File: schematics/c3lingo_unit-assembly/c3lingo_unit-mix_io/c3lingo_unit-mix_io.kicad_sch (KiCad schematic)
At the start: 40 parts, among them J201 Stage Line-In, J202 Mix Line-Out, J203 PowerSupply, J204 Inputs, J205 Output, U201 LM833N, U202 DRV134PA, U203 LM833N

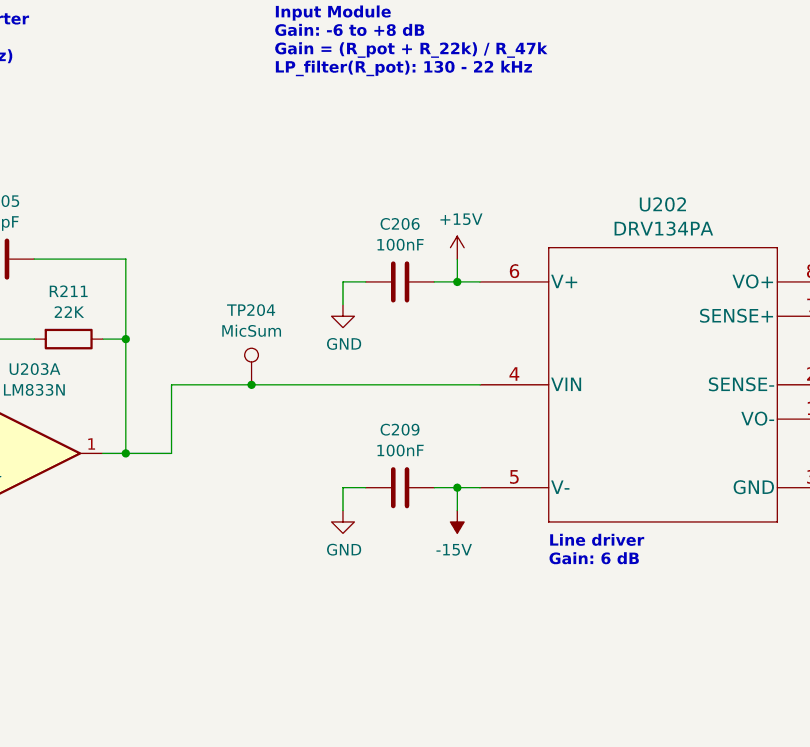
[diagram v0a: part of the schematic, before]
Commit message: Schematics: Fix multiple issues with initial prototype
- Removed high-pass filter between microphone pre-amp and gain as it made things sound worse
- Removed low-pass filter before VU meter as it looked fine without
- Connect VU meter to +15 V directly as 5 V didn't work
- Footprint of the gain potentiometer (Alps RK09) seems to be fixed with the KiCad 6 library
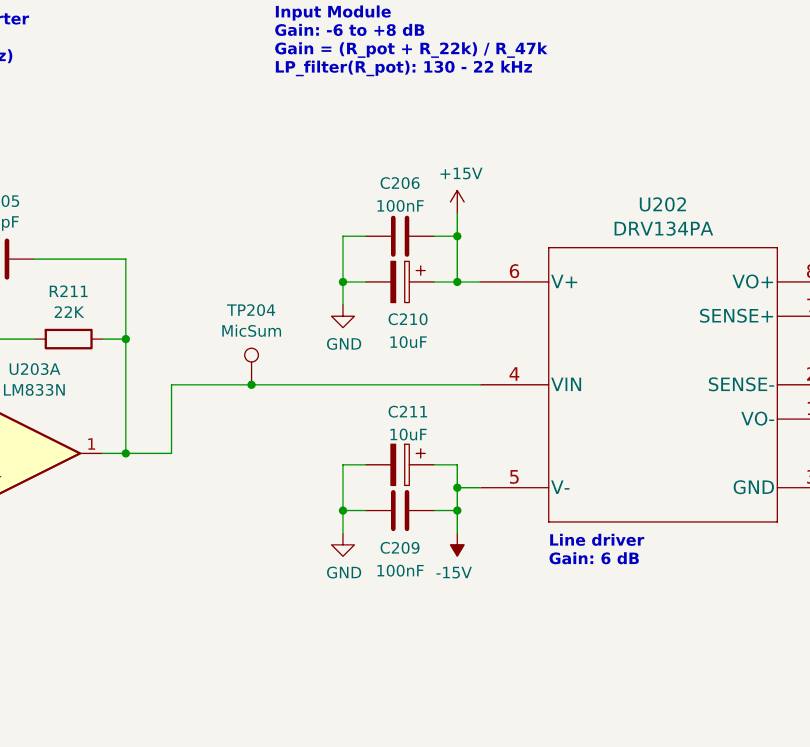
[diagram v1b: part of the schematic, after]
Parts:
- added C210, C211: 10uF, Capacitor_THT:CP_Radial_D5.0mm_P2.00mm, symbol Device:C_Polarized
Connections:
- net +15V: now also C210.1
- net -15V: now also C211.1
- net GND: now also C210.2, C211.2
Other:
- moved on the sheet: C206, C209

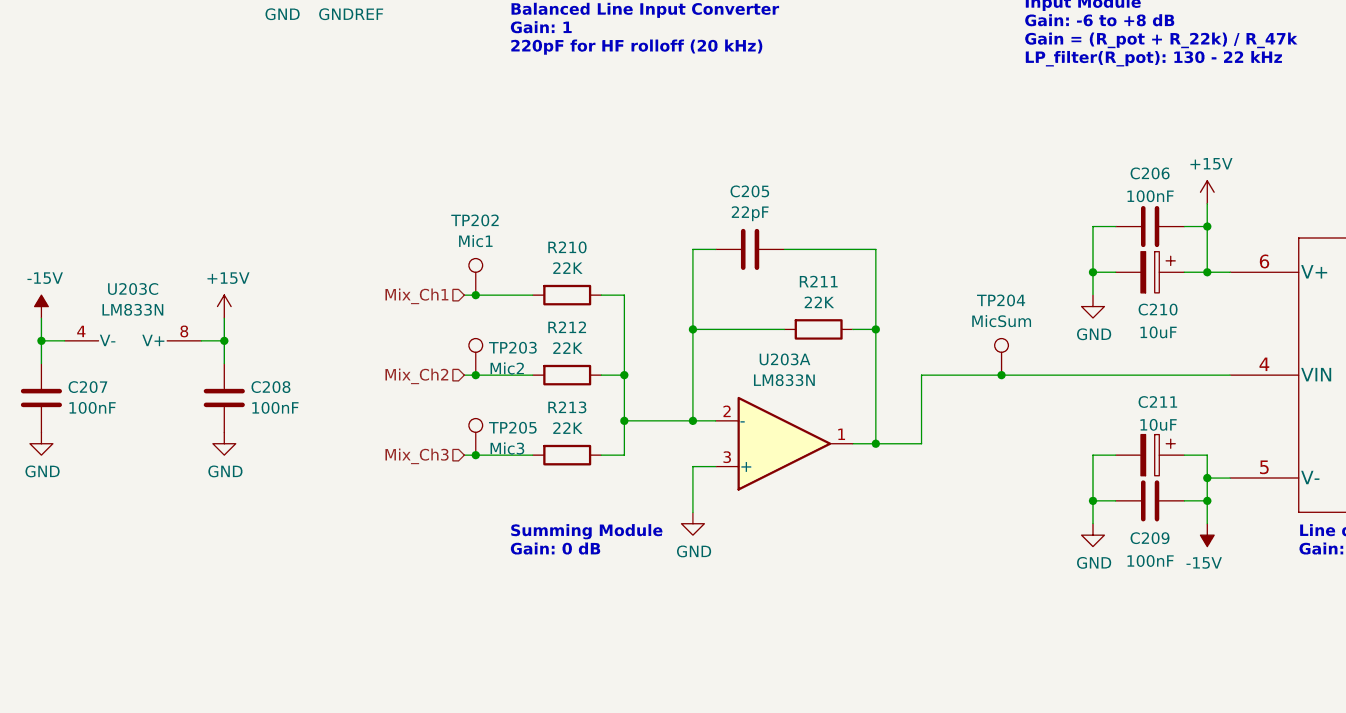
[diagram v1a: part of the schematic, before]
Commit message: [TIDY] Split channel into two schematics
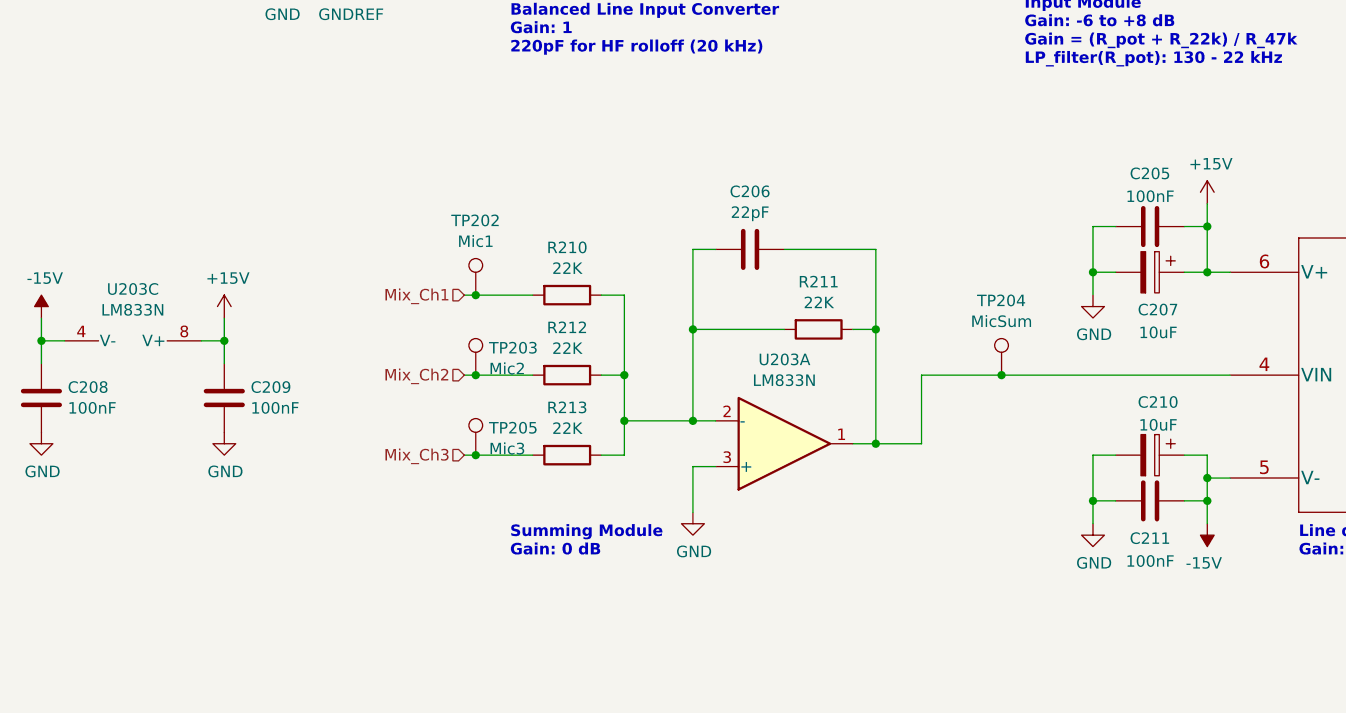
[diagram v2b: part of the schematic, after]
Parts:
- U202: footprint Package_DIP:DIP-8_W7.62mm_Socket_LongPads -> Package_DIP:DIP-8_W7.62mm
- renumbered C206 to C205, C205 to C206, C210 to C207, C207 to C208, C208 to C209, C211 to C210, C209 to C211
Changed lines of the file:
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@@
   (symbol (lib_id "Device:C") (at 27.94 116.84 180) (unit 1)
     (in_bom yes) (on_board yes)
-    (property "Reference" "C207" (id 0) (at 30.861 115.6716 0)
+    (property "Reference" "C208" (id 0) (at 30.861 115.6716 0)
       (effects (font (size 1.27 1.27)) (justify right))
     )
@@
   (symbol (lib_id "Device:C") (at 48.26 116.84 180) (unit 1)
     (in_bom yes) (on_board yes)
-    (property "Reference" "C208" (id 0) (at 51.181 115.6716 0)
+    (property "Reference" "C209" (id 0) (at 51.181 115.6716 0)
       (effects (font (size 1.27 1.27)) (justify right))
     )
@@
   (symbol (lib_id "Device:C") (at 106.68 100.33 270) (unit 1)
     (in_bom yes) (on_board yes)
-    (property "Reference" "C205" (id 0) (at 106.68 93.9292 90))
+    (property "Reference" "C206" (id 0) (at 106.68 93.9292 90))
     (property "Value" "22pF" (id 1) (at 106.68 96.2406 90))
     (property "Footprint" "Capacitor_THT:C_Disc_D5.0mm_W2.5mm_P5.00mm" (id 2) (at 102.87 101.2952 0)
@@
   (symbol (lib_id "power:GND") (at 100.33 129.54 0) (unit 1)
     (in_bom yes) (on_board yes)
-    (property "Reference" "#PWR0220" (id 0) (at 100.33 135.89 0)
+    (property "Reference" "#PWR0218" (id 0) (at 100.33 135.89 0)
       (effects (font (size 1.27 1.27)) hide)
     )
@@
       (effects (font (size 1.524 1.524)))
     )
-    (property "Footprint" "Package_DIP:DIP-8_W7.62mm_Socket_LongPads" (id 2) (at 180.34 98.044 0)
+    (property "Footprint" "Package_DIP:DIP-8_W7.62mm" (id 2) (at 180.34 98.044 0)
       (effects (font (size 1.524 1.524)) hide)
     )
@@
   (symbol (lib_id "power:-15V") (at 157.48 130.81 180) (unit 1)
     (in_bom yes) (on_board yes)
-    (property "Reference" "#PWR0218" (id 0) (at 157.48 133.35 0)
+    (property "Reference" "#PWR0220" (id 0) (at 157.48 133.35 0)
       (effects (font (size 1.27 1.27)) hide)
     )
@@
   (symbol (lib_id "power:GND") (at 144.78 130.81 0) (unit 1)
     (in_bom yes) (on_board yes)
-    (property "Reference" "#PWR0217" (id 0) (at 144.78 137.16 0)
+    (property "Reference" "#PWR0219" (id 0) (at 144.78 137.16 0)
       (effects (font (size 1.27 1.27)) hide)
     )
@@
   (symbol (lib_id "Device:C") (at 151.13 128.27 270) (unit 1)
     (in_bom yes) (on_board yes) (fields_autoplaced)
-    (property "Reference" "C209" (id 0) (at 151.13 132.4594 90))
+    (property "Reference" "C211" (id 0) (at 151.13 132.4594 90))
     (property "Value" "100nF" (id 1) (at 151.13 134.9963 90))
     (property "Footprint" "Capacitor_THT:C_Disc_D5.0mm_W2.5mm_P5.00mm" (id 2) (at 147.32 129.2352 0)
@@
   (symbol (lib_id "Device:C") (at 151.13 97.79 270) (unit 1)
     (in_bom yes) (on_board yes) (fields_autoplaced)
-    (property "Reference" "C206" (id 0) (at 151.13 91.9312 90))
+    (property "Reference" "C205" (id 0) (at 151.13 91.9312 90))
     (property "Value" "100nF" (id 1) (at 151.13 94.4681 90))
     (property "Footprint" "Capacitor_THT:C_Disc_D5.0mm_W2.5mm_P5.00mm" (id 2) (at 147.32 98.7552 0)
@@
   (symbol (lib_id "power:GND") (at 203.2 128.27 0) (unit 1)
     (in_bom yes) (on_board yes)
-    (property "Reference" "#PWR0219" (id 0) (at 203.2 134.62 0)
+    (property "Reference" "#PWR0217" (id 0) (at 203.2 134.62 0)
       (effects (font (size 1.27 1.27)) hide)
     )
@@
   (symbol (lib_id "Device:C_Polarized") (at 151.13 123.19 270) (unit 1)
     (in_bom yes) (on_board yes) (fields_autoplaced)
-    (property "Reference" "C211" (id 0) (at 152.019 117.3312 90))
+    (property "Reference" "C210" (id 0) (at 152.019 117.3312 90))
     (property "Value" "10uF" (id 1) (at 152.019 119.8681 90))
     (property "Footprint" "Capacitor_THT:CP_Radial_D5.0mm_P2.00mm" (id 2) (at 147.32 124.1552 0)
@@
   (symbol (lib_id "Device:C_Polarized") (at 151.13 102.87 270) (unit 1)
     (in_bom yes) (on_board yes) (fields_autoplaced)
-    (property "Reference" "C210" (id 0) (at 152.019 107.0594 90))
+    (property "Reference" "C207" (id 0) (at 152.019 107.0594 90))
     (property "Value" "10uF" (id 1) (at 152.019 109.5963 90))
     (property "Footprint" "Capacitor_THT:CP_Radial_D5.0mm_P2.00mm" (id 2) (at 147.32 103.8352 0)
@@
       (reference "C204") (unit 1) (value "100nF") (footprint "Capacitor_THT:C_Disc_D5.0mm_W2.5mm_P5.00mm")
     )
+    (path "/00000000-0000-0000-0000-0000604659b0"
+      (reference "C205") (unit 1) (value "100nF") (footprint "Capacitor_THT:C_Disc_D5.0mm_W2.5mm_P5.00mm")
+    )
     (path "/00000000-0000-0000-0000-00005fd269db"
-      (reference "C205") (unit 1) (value "22pF") (footprint "Capacitor_THT:C_Disc_D5.0mm_W2.5mm_P5.00mm")
-    )
-    (path "/00000000-0000-0000-0000-0000604659b0"
-      (reference "C206") (unit 1) (value "100nF") (footprint "Capacitor_THT:C_Disc_D5.0mm_W2.5mm_P5.00mm")
+      (reference "C206") (unit 1) (value "22pF") (footprint "Capacitor_THT:C_Disc_D5.0mm_W2.5mm_P5.00mm")
+    )
+    (path "/9feded9d-6d07-46f0-97ed-4e08902d2588"
+      (reference "C207") (unit 1) (value "10uF") (footprint "Capacitor_THT:CP_Radial_D5.0mm_P2.00mm")
     )
     (path "/00000000-0000-0000-0000-00005fcf1264"
-      (reference "C207") (unit 1) (value "100nF") (footprint "Capacitor_THT:C_Disc_D5.0mm_W2.5mm_P5.00mm")
+      (reference "C208") (unit 1) (value "100nF") (footprint "Capacitor_THT:C_Disc_D5.0mm_W2.5mm_P5.00mm")
     )
     (path "/00000000-0000-0000-0000-00005fcf126a"
-      (reference "C208") (unit 1) (value "100nF") (footprint "Capacitor_THT:C_Disc_D5.0mm_W2.5mm_P5.00mm")
+      (reference "C209") (unit 1) (value "100nF") (footprint "Capacitor_THT:C_Disc_D5.0mm_W2.5mm_P5.00mm")
+    )
+    (path "/36f80211-7578-4f7e-b084-5c1e7cfd5788"
+      (reference "C210") (unit 1) (value "10uF") (footprint "Capacitor_THT:CP_Radial_D5.0mm_P2.00mm")
     )
     (path "/00000000-0000-0000-0000-000060444365"
-      (reference "C209") (unit 1) (value "100nF") (footprint "Capacitor_THT:C_Disc_D5.0mm_W2.5mm_P5.00mm")
+      (reference "C211") (unit 1) (value "100nF") (footprint "Capacitor_THT:C_Disc_D5.0mm_W2.5mm_P5.00mm")
     )
     (path "/00000000-0000-0000-0000-00006148253b"

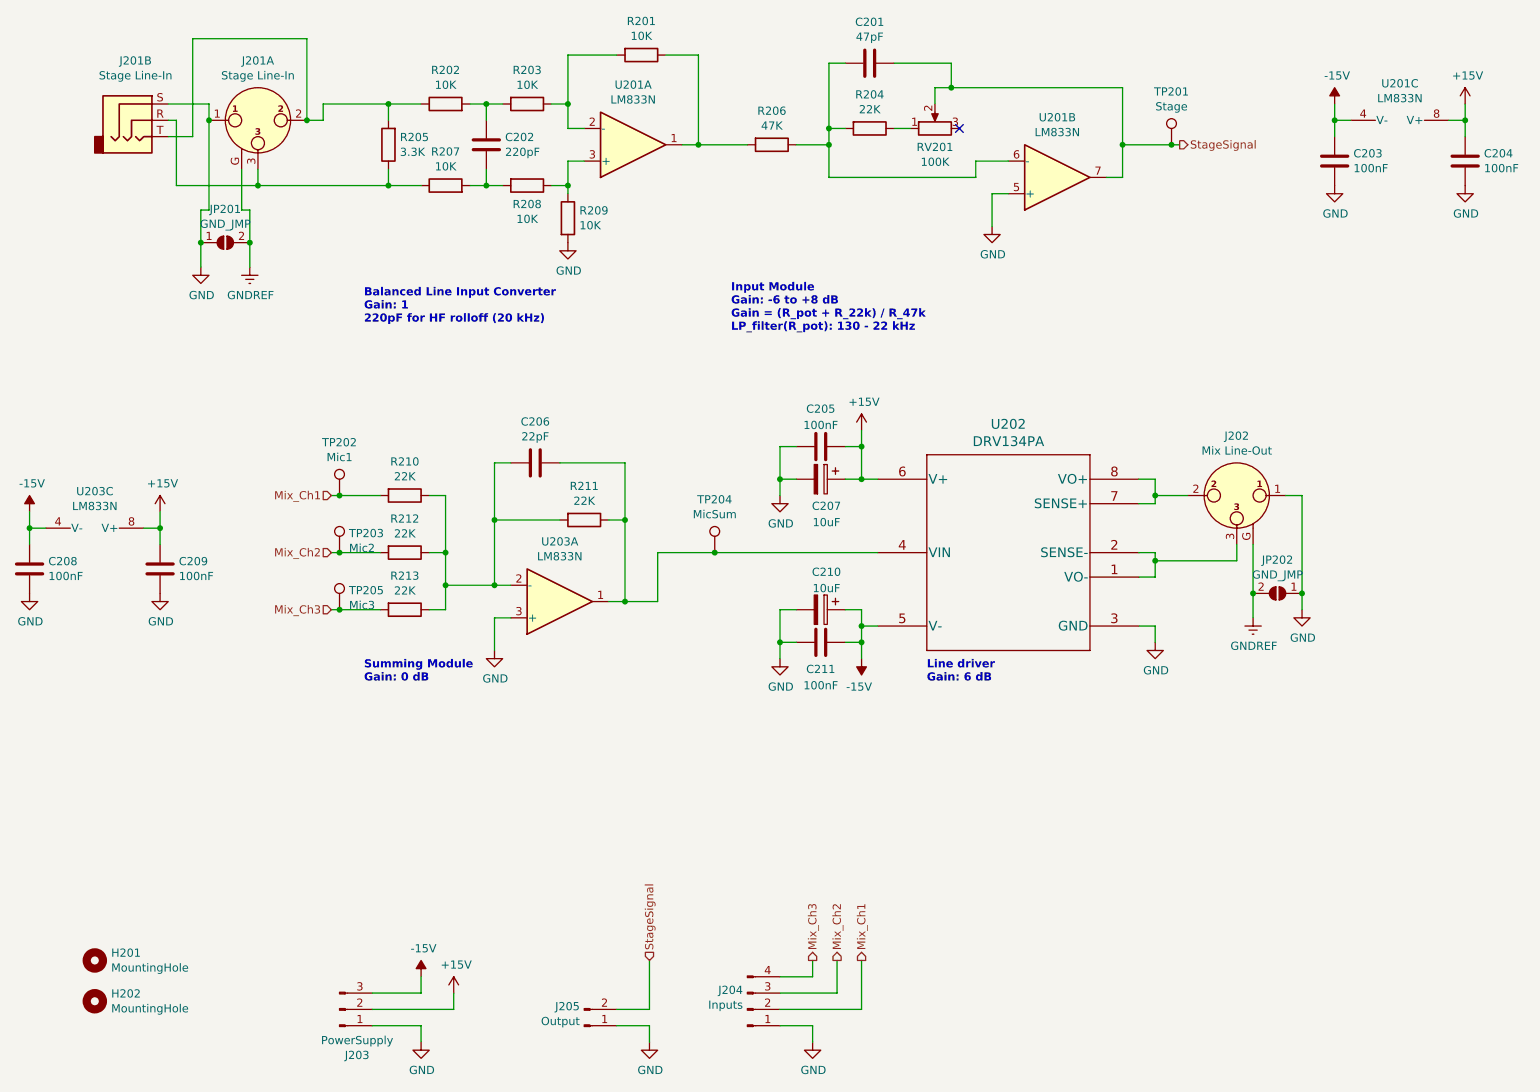
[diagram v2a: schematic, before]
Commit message: Update to KiCad 7
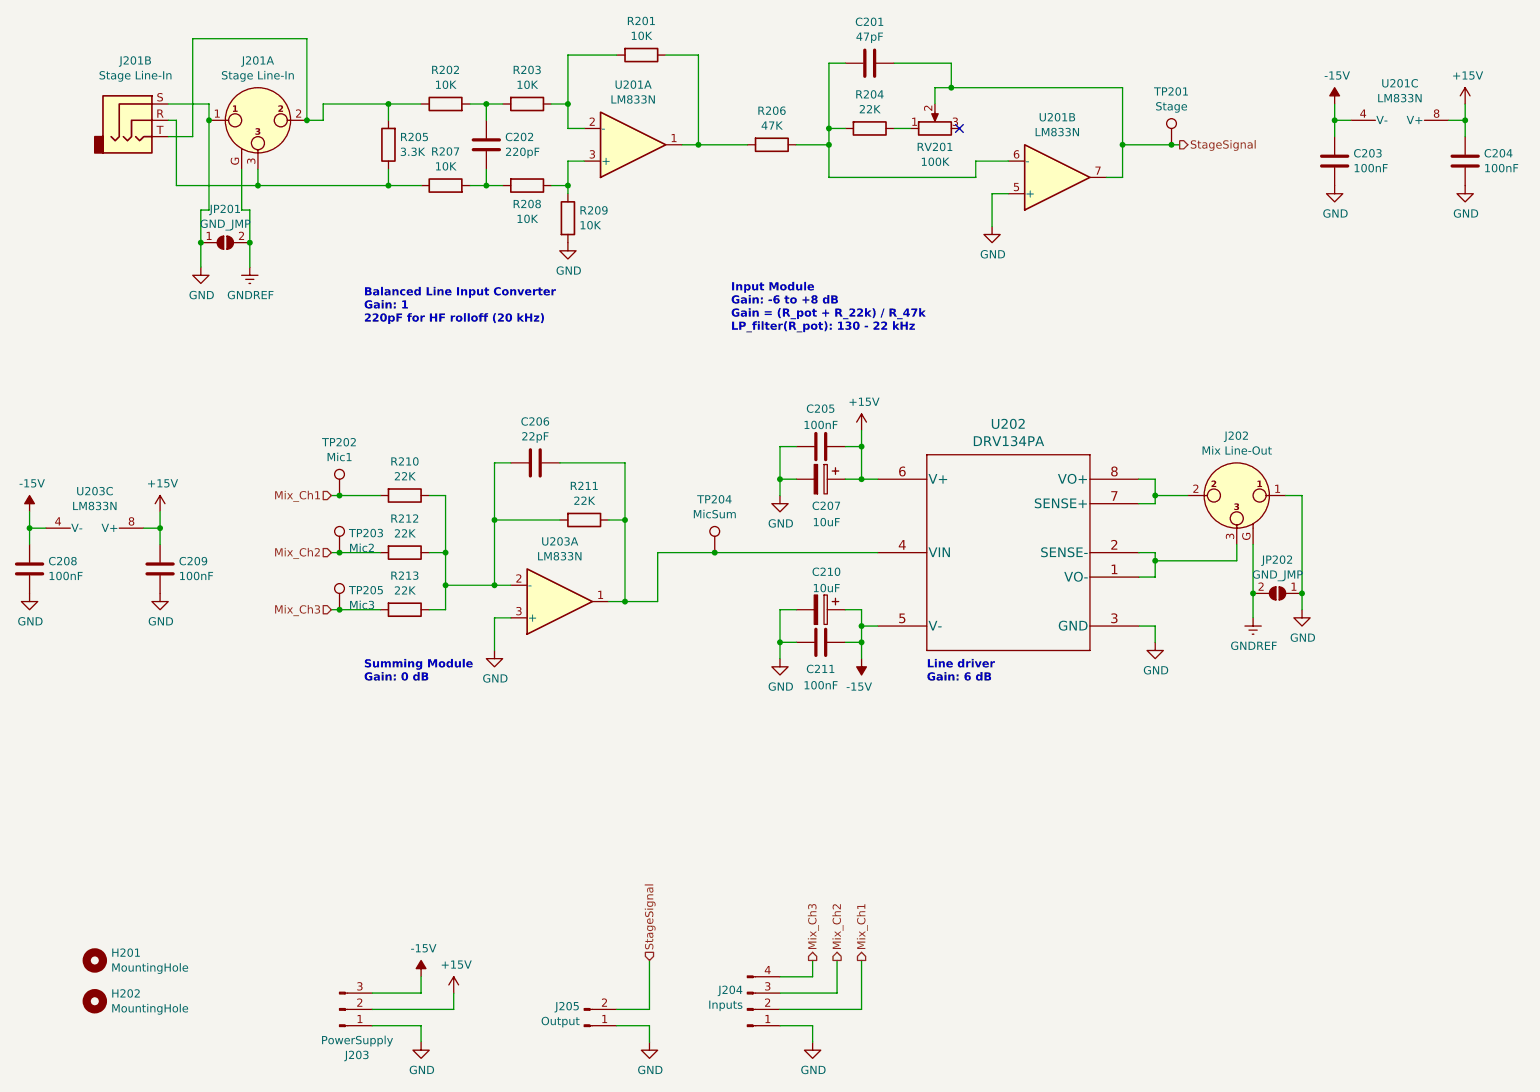
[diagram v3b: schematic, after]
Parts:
- J201: symbol Connector:XLR3_AudioJack3_Combo_Ground -> Connector_Audio:XLR3_AudioJack3_Combo_Ground
- J201: symbol Connector:XLR3_AudioJack3_Combo_Ground -> Connector_Audio:XLR3_AudioJack3_Combo_Ground; Model Combo XLR + 6.3 mm Jack -> NCJ6FA-H (Horiz. Combo Jack)
- J202: symbol Connector:XLR3_Ground -> Connector_Audio:XLR3_Ground
- J203: symbol Connector:Conn_01x03_Male -> Connector:Conn_01x03_Pin
- J204: symbol Connector:Conn_01x04_Male -> Connector:Conn_01x04_Pin
- J205: symbol Connector:Conn_01x02_Male -> Connector:Conn_01x02_Pin
